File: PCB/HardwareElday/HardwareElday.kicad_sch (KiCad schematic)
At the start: 13 parts, among them J1 Conn_01x04, J2 Conn_01x04, Q1 NMOS, Q2 NMOS, Q3 NPN, Q4 PNP, Q5 NMOS, Q6 NMOS

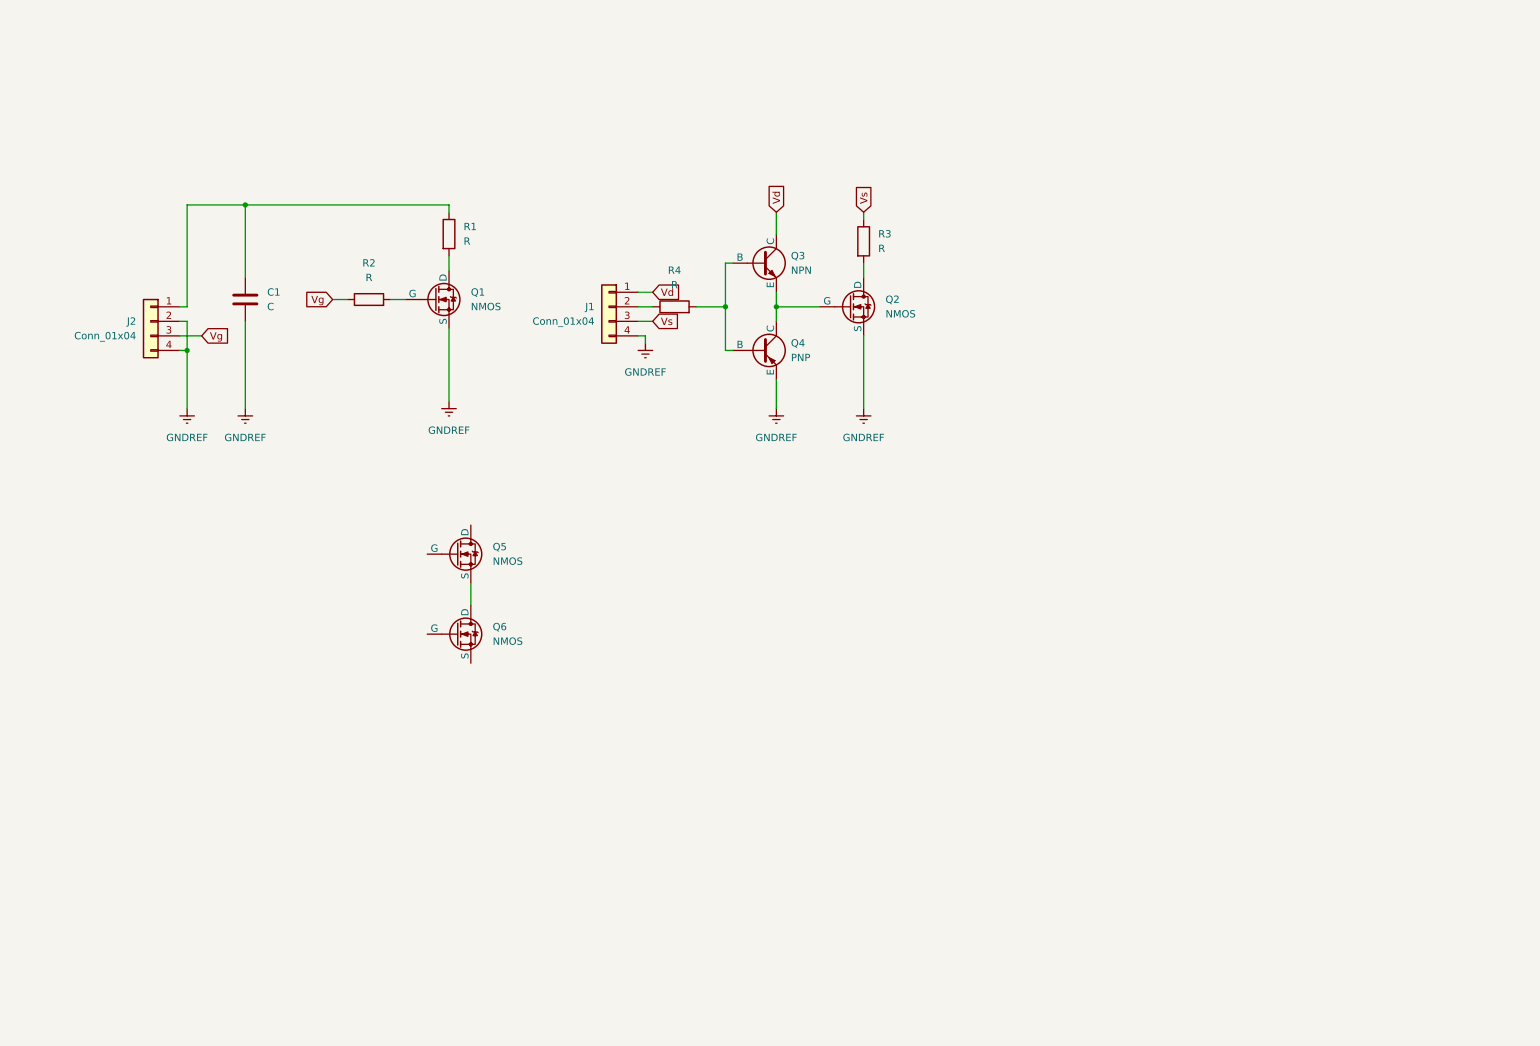
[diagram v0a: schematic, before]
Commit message: Update file report and simulation
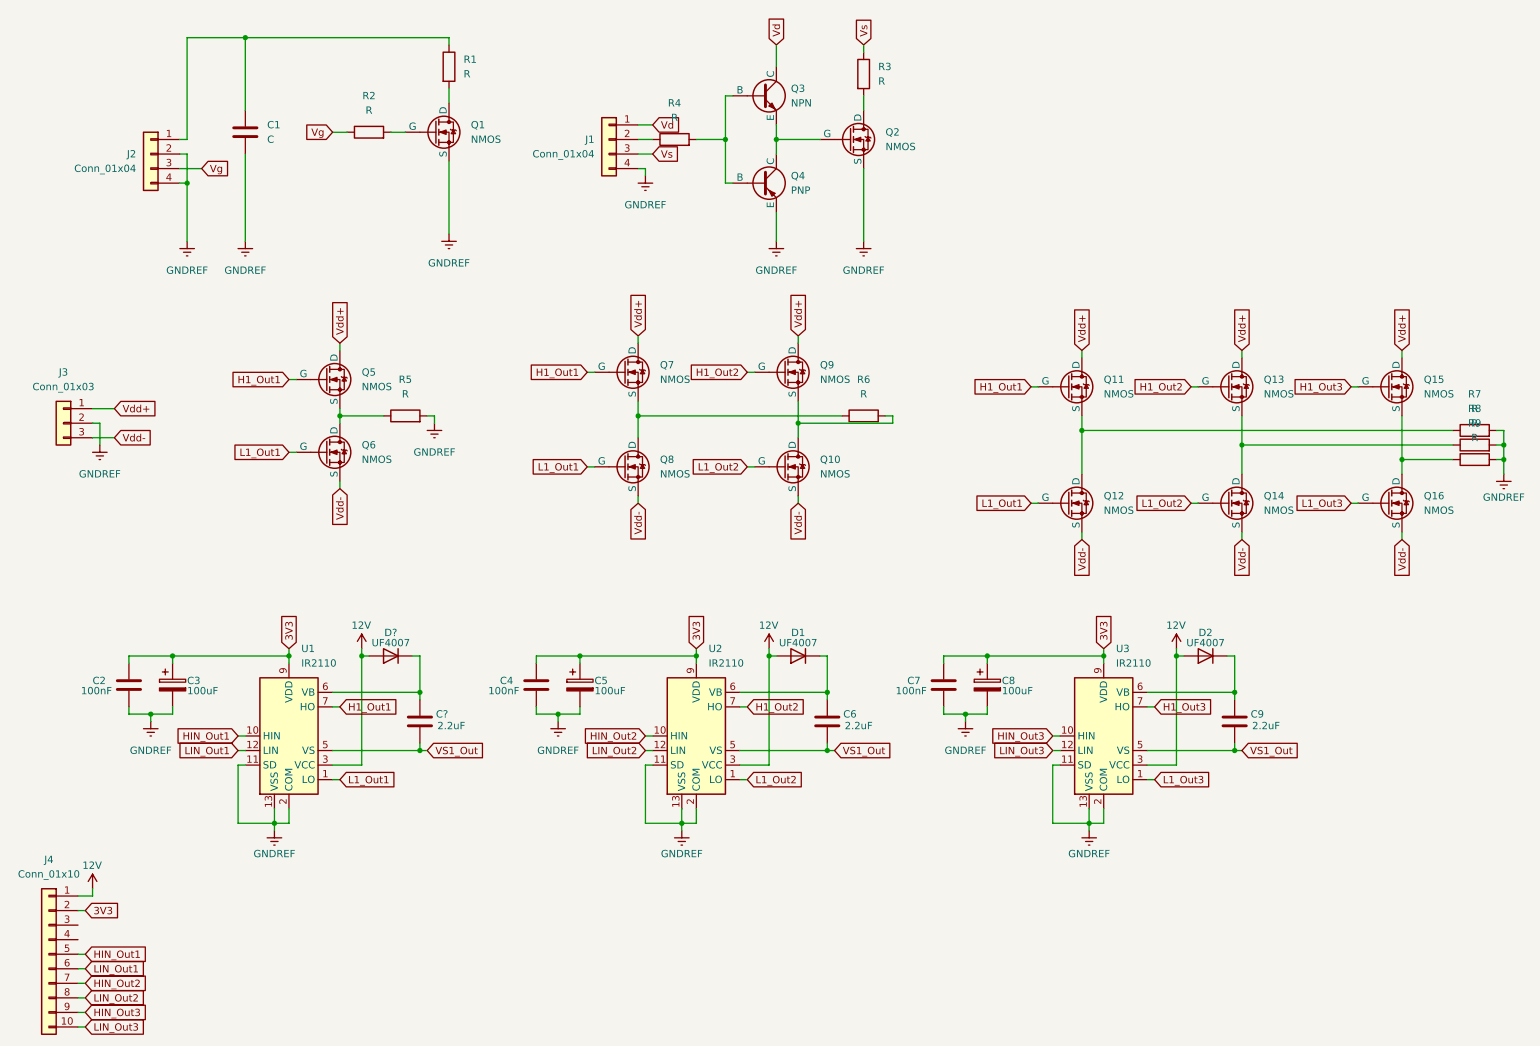
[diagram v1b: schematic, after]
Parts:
- added C2, C4, C7: 100nF, Capacitor_SMD:C_1206_3216Metric, symbol Device:C
- added C3, C5, C8: 100uF, Capacitor_SMD:CP_Elec_8x10, symbol Device:C_Polarized
- added C6, C9, C?: 2.2uF, Capacitor_SMD:C_1206_3216Metric, symbol Device:C
- added D1, D2, D?: UF4007, Diode_SMD:D_SMA, symbol Device:D
- added J3: Conn_01x03, symbol Connector_Generic:Conn_01x03
- added J4: Conn_01x10, symbol Connector_Generic:Conn_01x10
- added Q10, Q11, Q12, Q13, Q14, Q15, Q16, Q7, Q8, Q9: NMOS, symbol Simulation_SPICE:NMOS
- added R5, R6, R7, R8, R9: R, symbol Device:R
- added U1, U2, U3: IR2110, Package_DIP:DIP-14_W7.62mm, symbol Driver_FET:IR2110
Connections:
- net GNDREF: now also C2.2, C3.2, C4.2, C5.2, C7.2, C8.2, J3.2 (Pin_2), R5.2, R7.2, R8.2, R9.2, U1.11 (SD), U1.13 (VSS), U1.2 (COM), U2.11 (SD), U2.13 (VSS), U2.2 (COM), U3.11 (SD), U3.13 (VSS), U3.2 (COM)
- net at Q5.3 (S), Q6.1 (D): now also R5.1
- net L1_Out1: now reaches Q6.2 (G)
- net L1_Out1: now also Q12.2 (G), Q8.2 (G), U1.1 (LO)
- net Vdd-: now reaches Q6.3 (S)
- net Vdd-: now also J3.3 (Pin_3), Q10.3 (S), Q12.3 (S), Q14.3 (S), Q16.3 (S), Q8.3 (S)
- net Vdd+: now reaches Q5.1 (D)
- net Vdd+: now also J3.1 (Pin_1), Q11.1 (D), Q13.1 (D), Q15.1 (D), Q7.1 (D), Q9.1 (D)
- net H1_Out1: now reaches Q5.2 (G)
- net H1_Out1: now also Q11.2 (G), Q7.2 (G), U1.7 (HO)
- new net: C?.1, D?.1 (K), U1.6 (VB)
- new net: Q7.3 (S), Q8.1 (D), R6.1
- new net: Q15.3 (S), Q16.1 (D), R9.1
- new net: Q13.3 (S), Q14.1 (D), R8.1
- new net: C6.1, D1.1 (K), U2.6 (VB)
- new net: Q10.1 (D), Q9.3 (S), R6.2
- new net: C9.1, D2.1 (K), U3.6 (VB)
- new net: Q11.3 (S), Q12.1 (D), R7.1
- new net 12V: D1.2 (A), D2.2 (A), D?.2 (A), J4.1 (Pin_1), U1.3 (VCC), U2.3 (VCC), U3.3 (VCC)
- new net 3V3: C2.1, C3.1, C4.1, C5.1, C7.1, C8.1, J4.2 (Pin_2), U1.9 (VDD), U2.9 (VDD), U3.9 (VDD)
- new net H1_Out2: Q13.2 (G), Q9.2 (G), U2.7 (HO)
- new net H1_Out3: Q15.2 (G), U3.7 (HO)
- new net HIN_Out1: J4.5 (Pin_5), U1.10 (HIN)
- new net HIN_Out2: J4.7 (Pin_7), U2.10 (HIN)
- new net HIN_Out3: J4.9 (Pin_9), U3.10 (HIN)
- new net L1_Out2: Q10.2 (G), Q14.2 (G), U2.1 (LO)
- new net L1_Out3: Q16.2 (G), U3.1 (LO)
- new net LIN_Out1: J4.6 (Pin_6), U1.12 (LIN)
- new net LIN_Out2: J4.8 (Pin_8), U2.12 (LIN)
- new net LIN_Out3: J4.10 (Pin_10), U3.12 (LIN)
- new net VS1_Out: C6.2, C9.2, C?.2, U1.5 (VS), U2.5 (VS), U3.5 (VS)
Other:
- moved on the sheet: C1, J1, J2, Q1, Q2, Q3, Q4, Q5, Q6, R1, R2, R3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

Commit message: Update file report and simulation
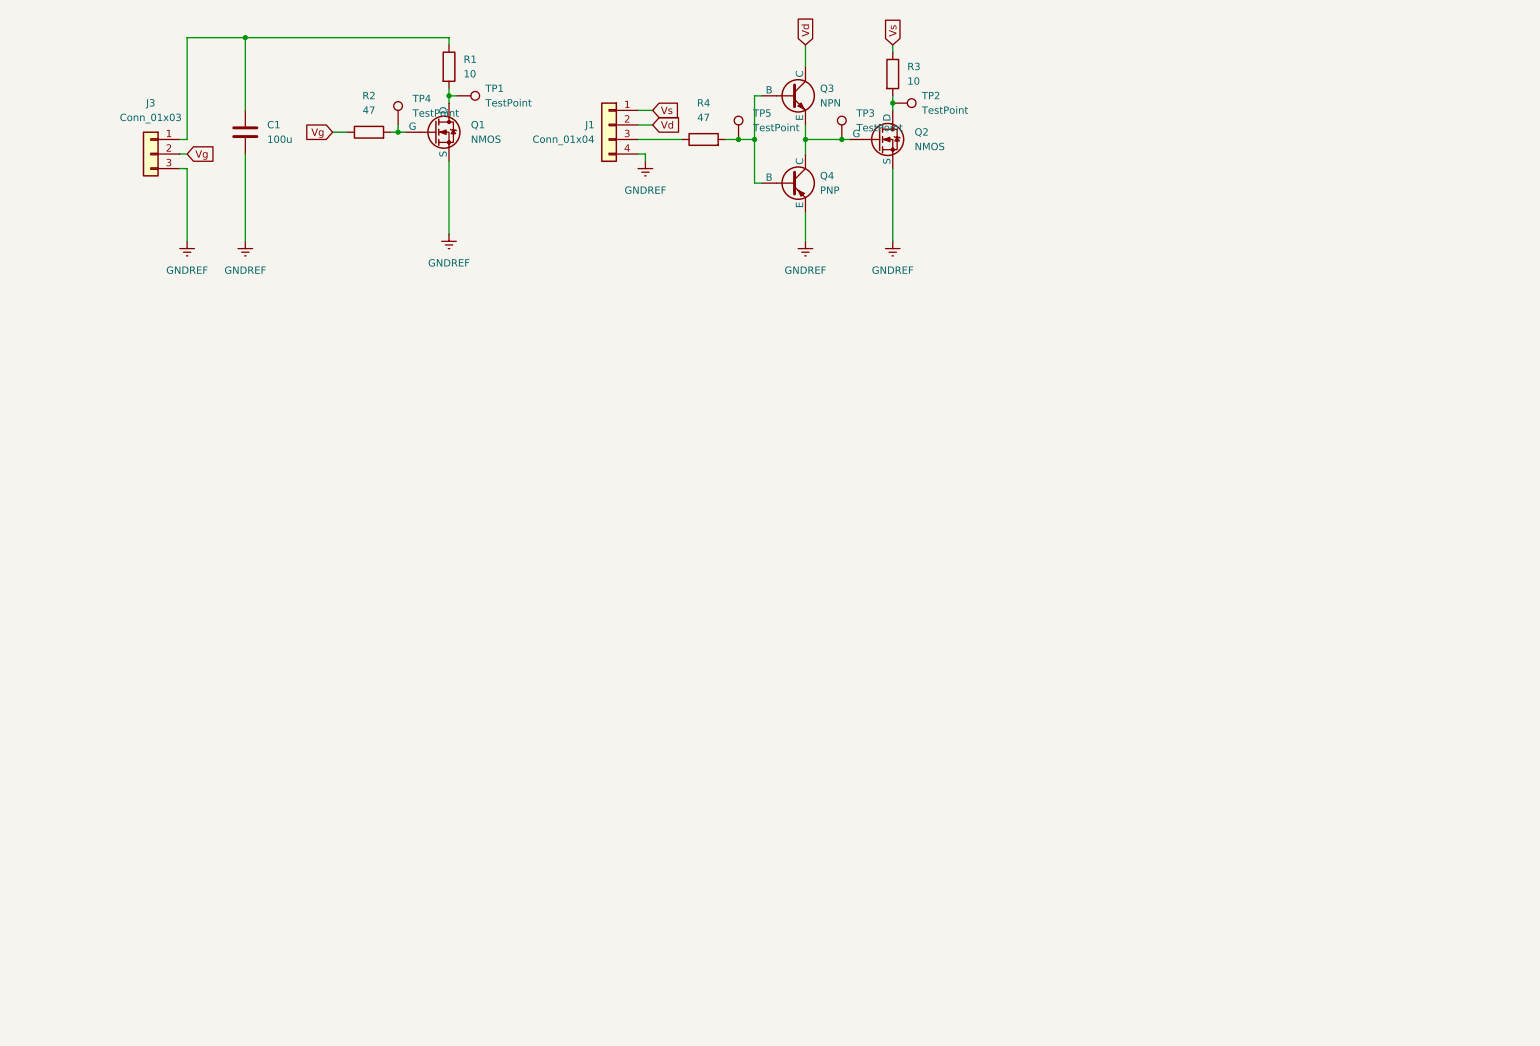
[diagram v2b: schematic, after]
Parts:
- removed C2, C4, C7: 100nF, Capacitor_SMD:C_1206_3216Metric, symbol Device:C
- removed C3, C5, C8: 100uF, Capacitor_SMD:CP_Elec_8x10, symbol Device:C_Polarized
- removed C6, C9, C?: 2.2uF, Capacitor_SMD:C_1206_3216Metric, symbol Device:C
- removed D1, D2, D?: UF4007, Diode_SMD:D_SMA, symbol Device:D
- removed J2: Conn_01x04, symbol Connector_Generic:Conn_01x04
- removed J4: Conn_01x10, symbol Connector_Generic:Conn_01x10
- removed Q10, Q11, Q12, Q13, Q14, Q15, Q16, Q5, Q6, Q7, Q8, Q9: NMOS, symbol Simulation_SPICE:NMOS
- removed R5, R6, R7, R8, R9: R, symbol Device:R
- removed U1, U2, U3: IR2110, Package_DIP:DIP-14_W7.62mm, symbol Driver_FET:IR2110
- added TP1, TP2, TP3, TP4, TP5: TestPoint, TestPoint:TestPoint_Loop_D2.60mm_Drill1.6mm_Beaded, symbol Connector:TestPoint
- C1: value C -> 100u; footprint (none) -> Capacitor_THT:CP_Radial_D6.3mm_P2.50mm
- J1: footprint (none) -> Connector_JST:JST_XH_B4B-XH-A_1x04_P2.50mm_Vertical
- J3: footprint (none) -> Connector_JST:JST_XH_B3B-XH-A_1x03_P2.50mm_Vertical
- Q1, Q2: footprint (none) -> Package_TO_SOT_THT:TO-220-3_Horizontal_TabDown
- Q3, Q4: footprint (none) -> Package_TO_SOT_THT:TO-92_Inline_Wide
- R1, R3: value R -> 10; footprint (none) -> Resistor_THT:R_Axial_DIN0411_L9.9mm_D3.6mm_P15.24mm_Horizontal
- R2, R4: value R -> 47; footprint (none) -> Resistor_THT:R_Axial_DIN0207_L6.3mm_D2.5mm_P10.16mm_Horizontal
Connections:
- net Vdd+ is gone; now on an unnamed net: J3.1 (Pin_1)
- net Vdd- is gone; now on net GNDREF: J3.3 (Pin_3)
- net GNDREF: no longer J3.2 (Pin_2)
- net Vd: now also J1.2 (Pin_2); no longer J1.1 (Pin_1)
- net Vg: now also J3.2 (Pin_2)
- net Vs: now also J1.1 (Pin_1); no longer J1.3 (Pin_3)
- net at Q2.2 (G), Q3.3 (E), Q4.1 (C): now also TP3.1
- net at Q3.2 (B), Q4.2 (B), R4.2: now also TP5.1
- net at Q1.1 (D), R1.2: now also TP1.1
- net at Q2.1 (D), R3.2: now also TP2.1
- net at Q1.2 (G), R2.2: now also TP4.1
- net at R4.1: now also J1.3 (Pin_3); no longer J1.2 (Pin_2)
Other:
- moved on the sheet: J1, Q2, Q3, Q4, R3, R4

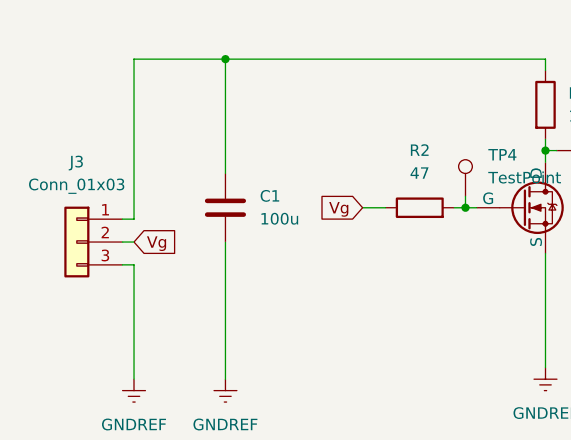
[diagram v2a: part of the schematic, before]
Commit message: Update file report and simulation
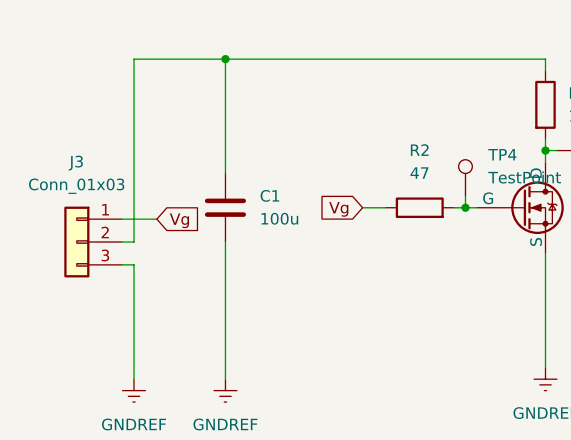
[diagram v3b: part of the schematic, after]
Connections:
- net GNDREF: now also Q4.1 (E); no longer Q4.3 (E)
- net Vd: now also Q3.2 (C); no longer Q3.1 (C)
- net Vg: now also J3.1 (Pin_1); no longer J3.2 (Pin_2)
- net at R4.2, TP5.1: now also Q3.3 (B), Q4.3 (B); no longer Q3.2 (B), Q4.2 (B)
- net at R2.2, TP4.1: now also Q1.1 (G); no longer Q1.2 (G)
- net at C1.1, R1.1: now also J3.2 (Pin_2); no longer J3.1 (Pin_1)
- net at R1.2, TP1.1: now also Q1.2 (D); no longer Q1.1 (D)
- net at R3.2, TP2.1: now also Q2.2 (D); no longer Q2.1 (D)
- new net: Q2.1 (G), Q3.1 (E), Q4.2 (C), TP3.1
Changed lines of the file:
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@@
+	)
+	(junction
+		(at 153.67 38.1)
+		(diameter 0)
+		(color 0 0 0 0)
 	)
 	(junction
@@
 	)
 	(junction
-		(at 153.67 38.1)
-		(diameter 0)
-		(color 0 0 0 0)
-	)
-	(junction
 		(at 168.91 31.75)
 		(diameter 0)
@@
 	(wire
 		(pts
-			(xy 45.72 38.1) (xy 44.45 38.1)
-		)
-		(stroke
-			(width 0)
-			(type default)
-		)
-	)
-	(wire
-		(pts
 			(xy 141.986 38.1) (xy 139.7 38.1)
 		)
@@
 	(wire
 		(pts
+			(xy 124.46 33.02) (xy 127 33.02)
+		)
+		(stroke
+			(width 0)
+			(type default)
+		)
+	)
+	(wire
+		(pts
+			(xy 168.91 30.48) (xy 168.91 31.75)
+		)
+		(stroke
+			(width 0)
+			(type default)
+		)
+	)
+	(wire
+		(pts
+			(xy 45.72 40.64) (xy 44.45 40.64)
+		)
+		(stroke
+			(width 0)
+			(type default)
+		)
+	)
+	(wire
+		(pts
+			(xy 91.44 30.48) (xy 91.44 31.75)
+		)
+		(stroke
+			(width 0)
+			(type default)
+		)
+	)
+	(wire
+		(pts
+			(xy 44.45 43.18) (xy 45.72 43.18)
+		)
+		(stroke
+			(width 0)
+			(type default)
+		)
+	)
+	(wire
+		(pts
+			(xy 44.45 38.1) (xy 48.26 38.1)
+		)
+		(stroke
+			(width 0)
+			(type default)
+		)
+	)
+	(wire
+		(pts
+			(xy 82.55 35.56) (xy 82.55 36.83)
+		)
+		(stroke
+			(width 0)
+			(type default)
+		)
+	)
+	(wire
+		(pts
+			(xy 91.44 41.91) (xy 91.44 54.61)
+		)
+		(stroke
+			(width 0)
+			(type default)
+		)
+	)
+	(wire
+		(pts
+			(xy 81.28 36.83) (xy 82.55 36.83)
+		)
+		(stroke
+			(width 0)
+			(type default)
+		)
+	)
+	(wire
+		(pts
+			(xy 45.72 20.32) (xy 45.72 40.64)
+		)
+		(stroke
+			(width 0)
+			(type default)
+		)
+	)
+	(wire
+		(pts
+			(xy 168.91 31.75) (xy 168.91 33.02)
+		)
+		(stroke
+			(width 0)
+			(type default)
+		)
+	)
+	(wire
+		(pts
+			(xy 144.78 38.1) (xy 141.986 38.1)
+		)
+		(stroke
+			(width 0)
+			(type default)
+		)
+	)
+	(wire
+		(pts
+			(xy 146.05 45.72) (xy 144.78 45.72)
+		)
+		(stroke
+			(width 0)
+			(type default)
+		)
+	)
+	(wire
+		(pts
+			(xy 91.44 29.21) (xy 91.44 30.48)
+		)
+		(stroke
+			(width 0)
+			(type default)
+		)
+	)
+	(wire
+		(pts
+			(xy 153.67 38.1) (xy 153.67 40.64)
+		)
+		(stroke
+			(width 0)
+			(type default)
+		)
+	)
+	(wire
+		(pts
+			(xy 55.88 40.64) (xy 55.88 55.88)
+		)
+		(stroke
+			(width 0)
+			(type default)
+		)
+	)
+	(wire
+		(pts
+			(xy 82.55 36.83) (xy 83.82 36.83)
+		)
+		(stroke
+			(width 0)
+			(type default)
+		)
+	)
+	(wire
+		(pts
 			(xy 153.67 35.56) (xy 153.67 38.1)
-		)
-		(stroke
-			(width 0)
-			(type default)
-		)
-	)
-	(wire
-		(pts
-			(xy 124.46 33.02) (xy 127 33.02)
-		)
-		(stroke
-			(width 0)
-			(type default)
-		)
-	)
-	(wire
-		(pts
-			(xy 168.91 30.48) (xy 168.91 31.75)
-		)
-		(stroke
-			(width 0)
-			(type default)
-		)
-	)
-	(wire
-		(pts
-			(xy 91.44 30.48) (xy 91.44 31.75)
-		)
-		(stroke
-			(width 0)
-			(type default)
-		)
-	)
-	(wire
-		(pts
-			(xy 44.45 43.18) (xy 45.72 43.18)
-		)
-		(stroke
-			(width 0)
-			(type default)
-		)
-	)
-	(wire
-		(pts
-			(xy 82.55 35.56) (xy 82.55 36.83)
-		)
-		(stroke
-			(width 0)
-			(type default)
-		)
-	)
-	(wire
-		(pts
-			(xy 91.44 41.91) (xy 91.44 54.61)
-		)
-		(stroke
-			(width 0)
-			(type default)
-		)
-	)
-	(wire
-		(pts
-			(xy 81.28 36.83) (xy 82.55 36.83)
-		)
-		(stroke
-			(width 0)
-			(type default)
-		)
-	)
-	(wire
-		(pts
-			(xy 45.72 38.1) (xy 45.72 20.32)
-		)
-		(stroke
-			(width 0)
-			(type default)
-		)
-	)
-	(wire
-		(pts
-			(xy 168.91 31.75) (xy 168.91 33.02)
-		)
-		(stroke
-			(width 0)
-			(type default)
-		)
-	)
-	(wire
-		(pts
-			(xy 144.78 38.1) (xy 141.986 38.1)
-		)
-		(stroke
-			(width 0)
-			(type default)
-		)
-	)
-	(wire
-		(pts
-			(xy 146.05 45.72) (xy 144.78 45.72)
-		)
-		(stroke
-			(width 0)
-			(type default)
-		)
-	)
-	(wire
-		(pts
-			(xy 91.44 29.21) (xy 91.44 30.48)
-		)
-		(stroke
-			(width 0)
-			(type default)
-		)
-	)
-	(wire
-		(pts
-			(xy 153.67 38.1) (xy 153.67 40.64)
-		)
-		(stroke
-			(width 0)
-			(type default)
-		)
-	)
-	(wire
-		(pts
-			(xy 55.88 40.64) (xy 55.88 55.88)
-		)
-		(stroke
-			(width 0)
-			(type default)
-		)
-	)
-	(wire
-		(pts
-			(xy 82.55 36.83) (xy 83.82 36.83)
-		)
-		(stroke
-			(width 0)
-			(type default)
-		)
-	)
-	(wire
-		(pts
-			(xy 45.72 40.64) (xy 44.45 40.64)
 		)
 		(stroke
@@
 	(global_label "Vg"
 		(shape input)
-		(at 45.72 40.64 0)
+		(at 48.26 38.1 0)
 		(fields_autoplaced yes)
 		(effects
@@
 		)
 		(property "Intersheetrefs" "${INTERSHEET_REFS}"
-			(at 50.9428 40.64 0)
+			(at 53.4828 38.1 0)
 			(effects
 				(font
@@
 			)
 		)
-		(property "Sim.Pins" "1=C 2=B 3=E"
+		(property "Sim.Pins" "2=C 3=B 1=E"
 			(at 151.13 45.72 0)
 			(effects
@@
 			)
 		)
-		(property "Sim.Pins" "1=C 2=B 3=E"
+		(property "Sim.Pins" "2=C 3=B 1=E"
 			(at 151.13 30.48 0)
 			(effects
@@
 	)
 	(symbol
+		(lib_name "NMOS_1")
 		(lib_id "Simulation_SPICE:NMOS")
 		(at 88.9 36.83 0)
@@
 			)
 		)
-		(property "Sim.Pins" "1=D 2=G 3=S"
+		(property "Sim.Pins" "2=D 1=G 3=S"
 			(at 88.9 52.07 0)
 			(effects
@@
 			)
 		)
-		(property "Sim.Pins" "1=D 2=G 3=S"
+		(property "Sim.Pins" "2=D 1=G 3=S"
 			(at 166.37 53.34 0)
 			(effects
